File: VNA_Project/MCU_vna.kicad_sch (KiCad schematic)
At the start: 11 parts, among them U2 STM32F100C6Tx, Y1 40 MHz crystal

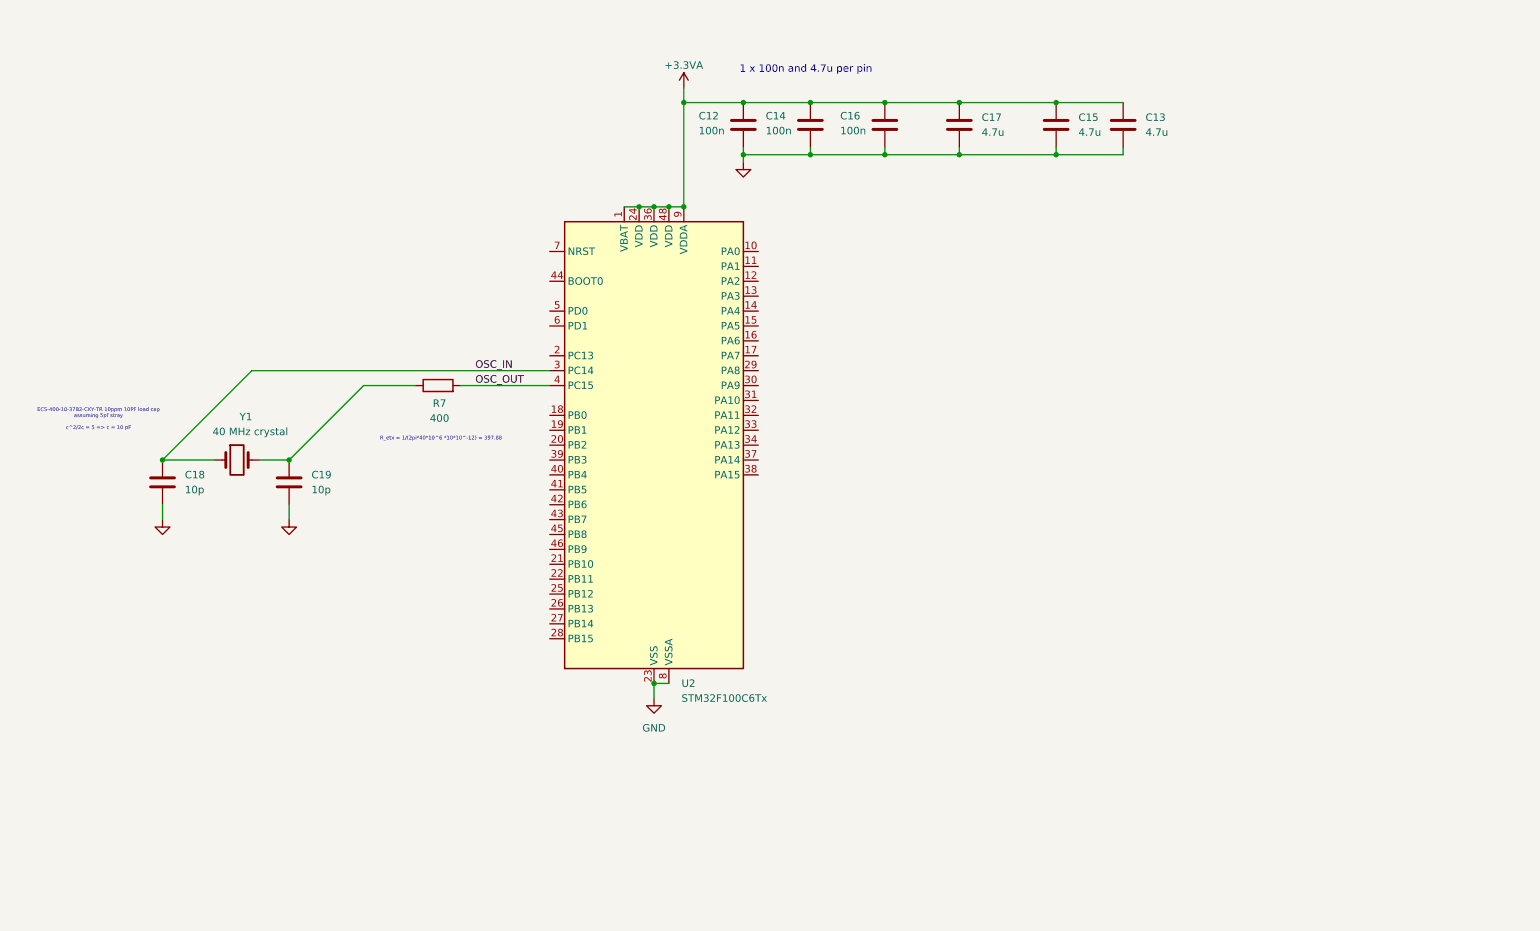
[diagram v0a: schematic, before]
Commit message: Added ESP32 MCU design
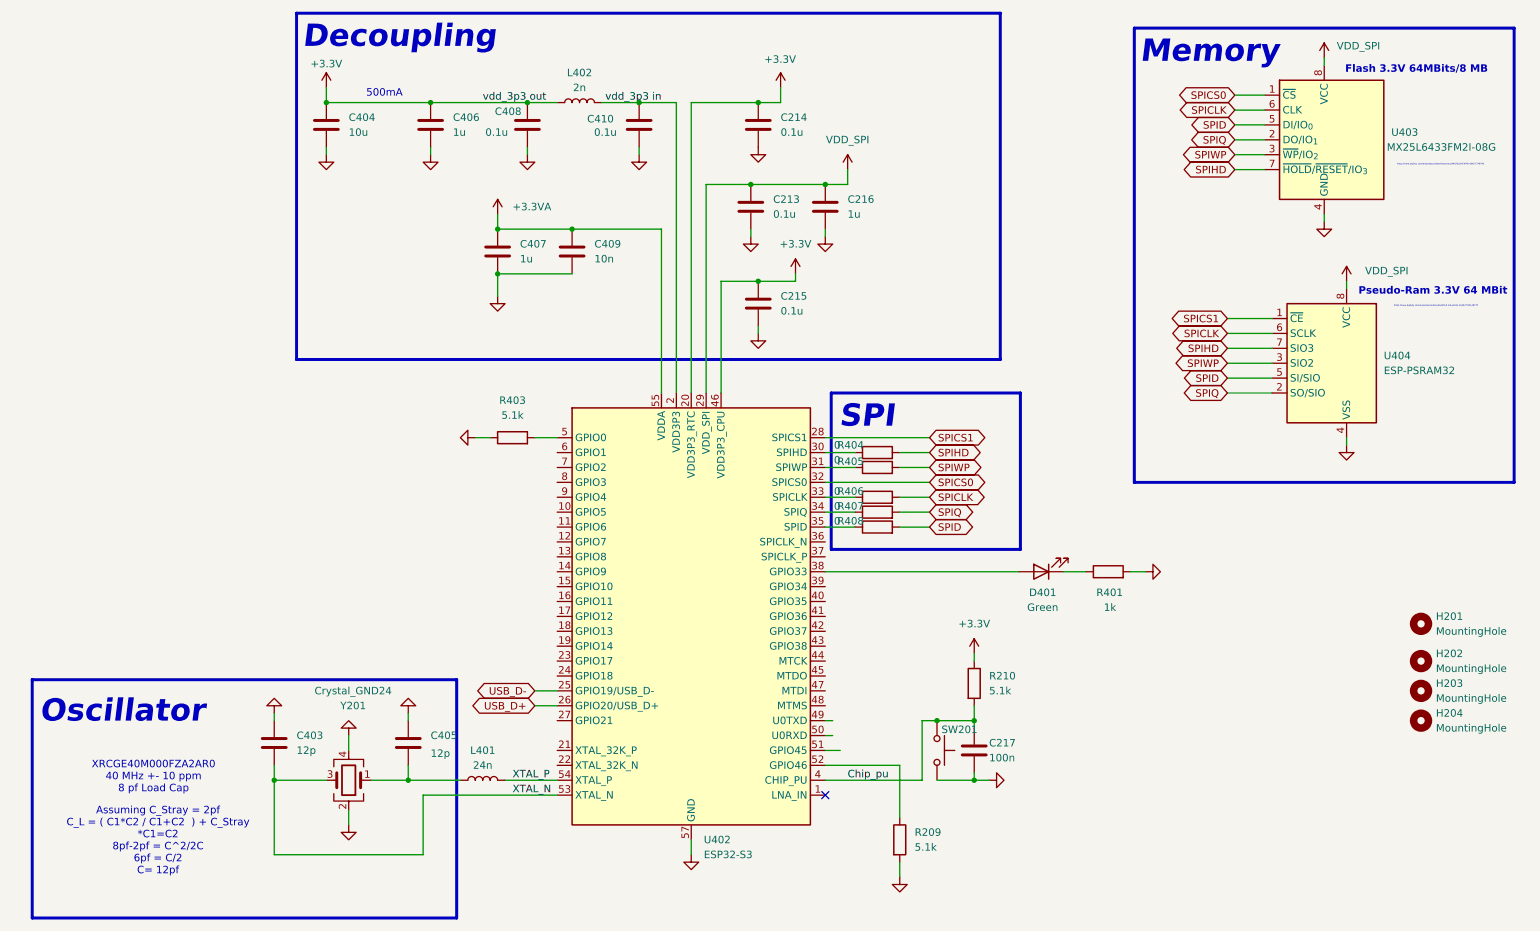
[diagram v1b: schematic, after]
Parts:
- removed C12, C14, C16: 100n, symbol Device:C
- removed C13, C15, C17: 4.7u, symbol Device:C
- removed C18, C19: 10p, symbol Device:C
- removed R7: 400, symbol Device:R
- removed U2: STM32F100C6Tx, Package_QFP:LQFP-48_7x7mm_P0.5mm, symbol MCU_ST_STM32F1:STM32F100C6Tx
- removed Y1: 40 MHz crystal, symbol Device:Crystal
- added C213, C214, C215, C408, C410: 0.1u, Capacitor_SMD:C_0402_1005Metric_Pad0.74x0.62mm_HandSolder, symbol Device:C
- added C216, C406, C407: 1u, Capacitor_SMD:C_0603_1608Metric_Pad1.08x0.95mm_HandSolder, symbol Device:C
- added C217: 100n, Capacitor_SMD:C_0402_1005Metric_Pad0.74x0.62mm_HandSolder, symbol Device:C
- added C403, C405: 12p, Capacitor_SMD:C_0402_1005Metric_Pad0.74x0.62mm_HandSolder, symbol Device:C
- added C404: 10u, Capacitor_SMD:C_0603_1608Metric_Pad1.08x0.95mm_HandSolder, symbol Device:C
- added C409: 10n, Capacitor_SMD:C_0402_1005Metric_Pad0.74x0.62mm_HandSolder, symbol Device:C
- added D401: Green, symbol Device:LED
- added H201, H202, H203, H204: MountingHole, MountingHole:MountingHole_3.2mm_M3, symbol Mechanical:MountingHole
- added L401: 24n, Inductor_SMD:L_0402_1005Metric_Pad0.77x0.64mm_HandSolder, symbol Device:L
- added L402: 2n, Inductor_SMD:L_0402_1005Metric_Pad0.77x0.64mm_HandSolder, symbol Device:L
- added R209, R210, R403: 5.1k, Resistor_SMD:R_0402_1005Metric_Pad0.72x0.64mm_HandSolder, symbol Device:R
- added R401: 1k, symbol Device:R
- added R404, R405, R406, R407, R408: 0, Resistor_SMD:R_0402_1005Metric_Pad0.72x0.64mm_HandSolder, symbol Device:R
- added SW201: SW_Push, Button_Switch_THT:SW_PUSH_6mm_H4.3mm, symbol Switch:SW_Push
- added U402: ESP32-S3, Package_DFN_QFN:QFN-56-1EP_7x7mm_P0.4mm_EP4x4mm, symbol MCU_Espressif:ESP32-S3
- added U403: MX25L6433FM2I-08G, Package_SO:SOIC-8_5.3x5.3mm_P1.27mm, symbol Memory_Flash:W25Q32JVSS
- added U404: ESP-PSRAM32, Package_SO:SOIC-8_3.9x4.9mm_P1.27mm, symbol Memory_RAM:ESP-PSRAM32
- added Y201: Crystal_GND24, Crystal:Crystal_SMD_SeikoEpson_FA128-4Pin_2.0x1.6mm, symbol Device:Crystal_GND24
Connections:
- net +3.3VA: now also C407.1, C409.1, U402.55 (VDDA), U402.56 (VDDA)
- net GND: now also C213.2, C214.2, C215.2, C216.2, C217.2, C403.2, C404.1, C405.2, C406.1, C407.2, C408.1, C409.2, C410.1, R209.2, R401.2, R403.1, SW201.2, U402.57 (GND), U403.4 (GND), U404.4 (VSS), Y201.2, Y201.4
- new net: R403.2, U402.5 (GPIO0)
- new net: C405.1, L401.1, Y201.1
- new net: R404.1, U402.30 (SPIHD)
- new net: R405.1, U402.31 (SPIWP)
- new net: R406.1, U402.33 (SPICLK)
- new net: R407.1, U402.34 (SPIQ)
- new net: R408.1, U402.35 (SPID)
- new net: D401.2 (A), U402.38 (GPIO33)
- new net: R209.1, U402.52 (GPIO46)
- new net: D401.1 (K), R401.1
- new net +3.3V: C214.1, C215.1, C404.2, C406.2, C408.2, L402.1, R210.1, U402.20 (VDD3P3_RTC), U402.46 (VDD3P3_CPU)
- new net Chip_pu: C217.1, R210.2, SW201.1, U402.4 (CHIP_PU)
- new net SPICLK: R406.2, U403.6 (CLK), U404.6 (SCLK)
- new net SPICS0: U402.32 (SPICS0), U403.1 (~{CS})
- new net SPICS1: U402.28 (SPICS1), U404.1 (~{CE})
- new net SPID: R408.2, U403.5 (DI/IO_{0}), U404.5 (SI/SIO)
- new net SPIHD: R404.2, U403.7 (~{HOLD}/~{RESET}/IO_{3}), U404.7 (SIO3)
- new net SPIQ: R407.2, U403.2 (DO/IO_{1}), U404.2 (SO/SIO)
- new net SPIWP: R405.2, U403.3 (~{WP}/IO_{2}), U404.3 (SIO2)
- new net USB_D+: U402.26 (GPIO20/USB_D+)
- new net USB_D-: U402.25 (GPIO19/USB_D-)
- new net VDD_SPI: C213.1, C216.1, U402.29 (VDD_SPI), U403.8 (VCC), U404.8 (VCC)
- new net XTAL_N: C403.1, U402.53 (XTAL_N), Y201.3
- new net XTAL_P: L401.2, U402.54 (XTAL_P)
- new net vdd_3p3 in: C410.2, L402.2, U402.2 (VDD3P3), U402.3 (VDD3P3)
- no-connect marks 0 -> 1
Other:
- note added: "500mA"
- note added: "Assuming C_Stray = 2pf C_L = ( C1*C2 / C1+C2 ) + C_Stray *C1=C2 8pf-2pf = C^2/2C 6pf = C/2 C= 12pf"
- note added: "Decoupling"
- note added: "Flash 3.3V 64MBits/8 MB"
- note added: "Memory"
- note added: "Oscillator"
- note added: "Pseudo-Ram 3.3V 64 MBit"
- note added: "SPI"
- note added: "XRCGE40M000FZA2AR0 40 MHz +- 10 ppm 8 pf Load Cap"
- note added: "https://www.digikey.com/en/products/detail/adafruit-industries-llc/4677/13148775"
- note added: "https://www.digikey.com/en/products/detail/macronix/MX25L6433FM2I-08G/7796740"
- note removed: "1 x 100n and 4.7u per pin"
- note removed: "ECS-400-10-37B2-CKY-TR 10ppm 10PF load cap assuming 5pf stray c^2/2c = 5 => c = 10 pF"
- note removed: "R_etx = 1/(2pi*40*10^6 *10*10^-12) = 397.88"
